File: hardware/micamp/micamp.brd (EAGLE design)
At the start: 16.5 x 10.2 mm, 14 parts, among them M1 MIC9.7MM, U1 OPA344

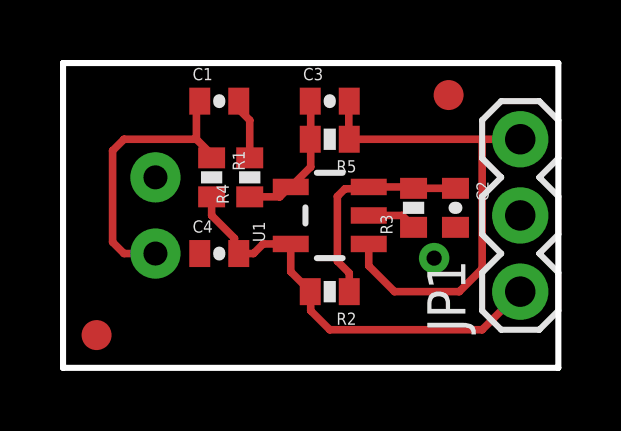
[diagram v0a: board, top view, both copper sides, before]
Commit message: switch to 0603 package which is still hand-solderable
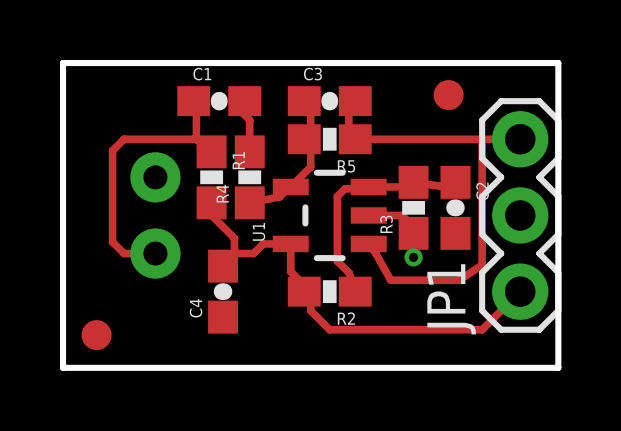
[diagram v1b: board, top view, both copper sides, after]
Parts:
- C1, C2, C3, C4: device SparkFun:0402-CAP -> SparkFun:0603-CAP
- R1, R2, R3, R4, R5: device SparkFun:0402-RES -> SparkFun:0603-RES
- moved C4 1.28 mm to (5.33, 2.54), turned to 90 degrees
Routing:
- net N$2: track 4.67 -> 5.27 mm
- net VCC: track 15.1 -> 15.6 mm
- net AUD: track 16.6 -> 16.1 mm
